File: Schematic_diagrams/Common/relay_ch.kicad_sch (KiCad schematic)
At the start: 9 parts

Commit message: updates to rev B
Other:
- company: Amberley Museum - Billingshurst Signal Box -> Amerley Museum - Billingshurst Signalbox
- title: Relay Module - Single Channel -> Track Diagram Lamp Controller
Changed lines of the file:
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@@
 	(paper "A4")
 	(title_block
-		(title "Relay Module - Single Channel")
-		(date "2026-02-09")
-		(rev "A")
-		(company "Amberley Museum - Billingshurst Signal Box")
+		(title "Track Diagram Lamp Controller")
+		(date "07/02/2026")
+		(rev "B")
+		(company "Amerley Museum - Billingshurst Signalbox")
 	)
 	(text_box "Channel 1 of 8-channel relay module pcb\n- only ch 1 shown for clarity\n(channel 8 is spare)"

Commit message: Amberley spelling corrected
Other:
- company: Amerley Museum - Billingshurst Signalbox -> Amberley Museum - Billingshurst Signalbox
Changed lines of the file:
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@@
 		(date "07/02/2026")
 		(rev "B")
-		(company "Amerley Museum - Billingshurst Signalbox")
+		(company "Amberley Museum - Billingshurst Signalbox")
 	)
 	(text_box "Channel 1 of 8-channel relay module pcb\n- only ch 1 shown for clarity\n(channel 8 is spare)"

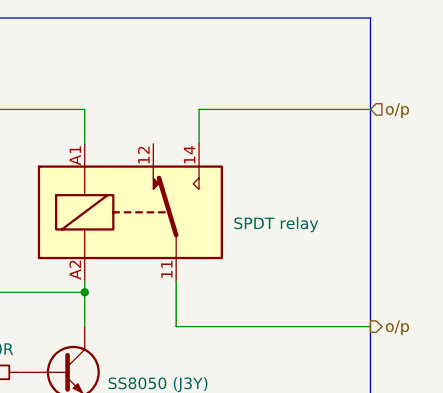
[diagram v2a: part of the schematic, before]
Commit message: general changes
update to relay module input name
new schematic: internal signal box model signal control
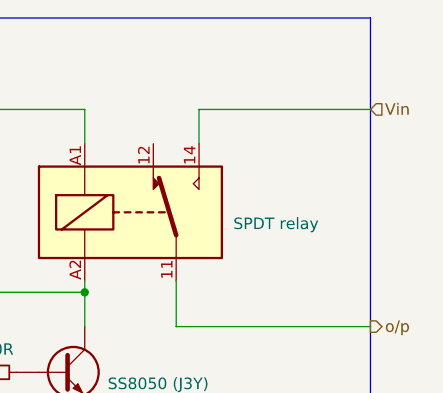
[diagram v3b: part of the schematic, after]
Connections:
- net o/p: no longer K?.14
- new net Vin: K?.14
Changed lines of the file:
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@@
 		)
 	)
-	(hierarchical_label "o{slash}p"
+	(hierarchical_label "Vin"
 		(shape input)
 		(at 187.96 62.23 0)
